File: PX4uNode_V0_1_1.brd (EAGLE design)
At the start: 45.4 x 34 mm, 134 parts, among them M3_MOUNT1101 MOUNT-HOLE3.1MM, M3_MOUNT1102 MOUNT-HOLE3.1MM, M3_MOUNT1103 MOUNT-HOLE3.1MM, M3_MOUNT1104 MOUNT-HOLE3.1MM, U101 STM32F4X7VX, U401 MAX3051, U402 MAX3051, X101 3.2x2.5 mm / 24 MHz / 15 ppm

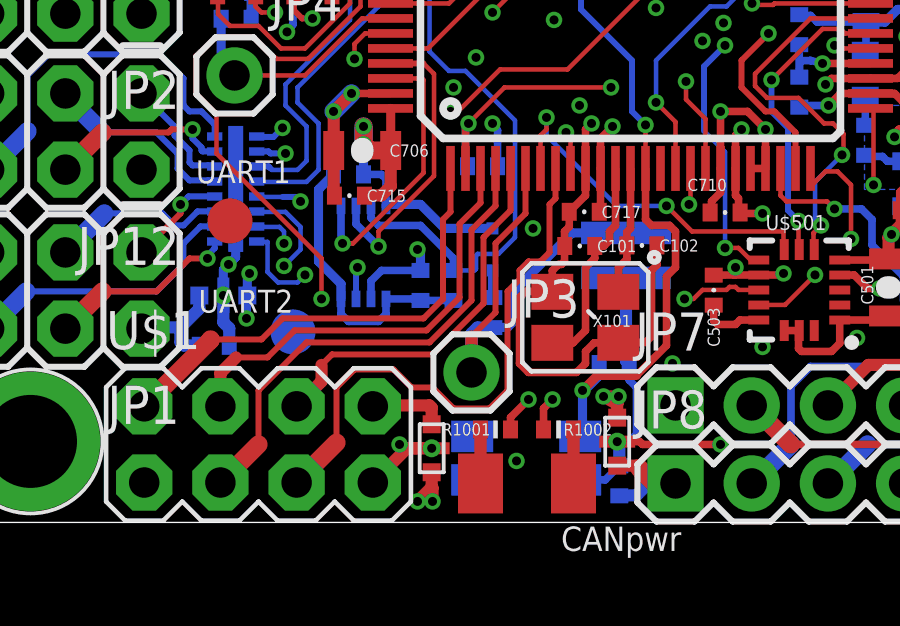
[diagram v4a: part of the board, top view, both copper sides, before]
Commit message: Removed extra Vbat hole
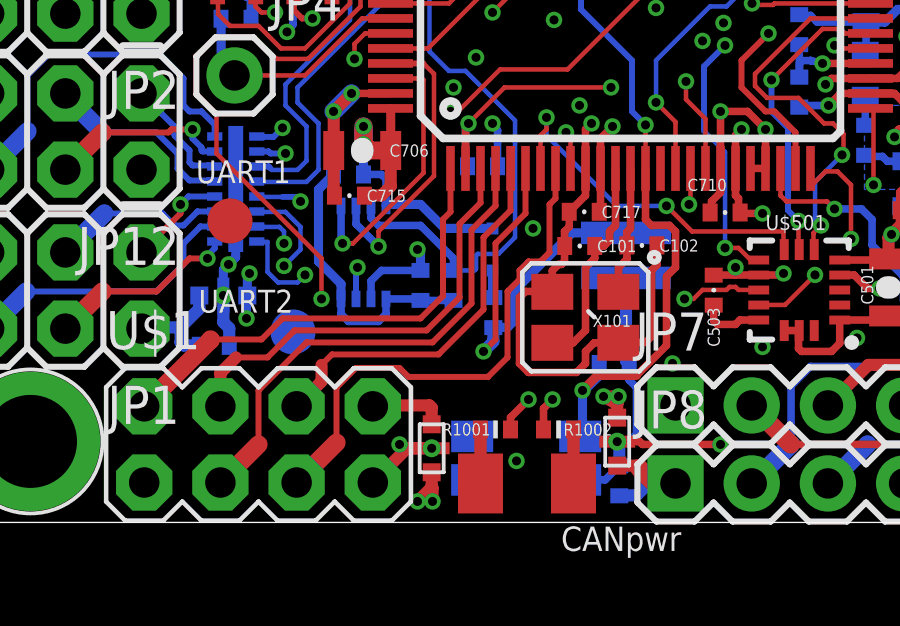
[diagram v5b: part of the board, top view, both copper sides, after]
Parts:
- removed JP3: M01PTH, SparkFun-Connectors:1X01
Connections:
- net VBAT: no longer JP3.1
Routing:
- net VBAT: track 16.0 -> 13.9 mm, vias 0 -> 1
- net GPIO_EXT_1: track 18.8 -> 17.3 mm
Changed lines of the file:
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@@
 <layer number="1" name="Top" color="4" fill="1" visible="yes" active="yes"/>
 <layer number="2" name="Ground" color="2" fill="10" visible="no" active="yes"/>
-<layer number="3" name="Horizontal" color="13" fill="15" visible="no" active="yes"/>
+<layer number="3" name="Horizontal" color="13" fill="15" visible="yes" active="yes"/>
 <layer number="4" name="Route4" color="1" fill="4" visible="no" active="no"/>
 <layer number="5" name="Route5" color="4" fill="4" visible="no" active="no"/>
@@
 <layer number="12" name="Route12" color="1" fill="5" visible="no" active="no"/>
 <layer number="13" name="Route13" color="4" fill="5" visible="no" active="no"/>
-<layer number="14" name="Vertical" color="14" fill="15" visible="no" active="yes"/>
+<layer number="14" name="Vertical" color="14" fill="15" visible="yes" active="yes"/>
 <layer number="15" name="Power" color="11" fill="15" visible="no" active="yes"/>
 <layer number="16" name="Bottom" color="1" fill="1" visible="yes" active="yes"/>
@@
 <attribute name="PARTNO" value="RC0402FR-0710KL" x="45.4" y="28.5" size="1.778" layer="27" rot="R180" display="off"/>
 </element>
-<element name="JP3" library="SparkFun-Connectors" package="1X01" value="M01PTH" x="30.2" y="9.2"/>
 <element name="JP4" library="SparkFun-Connectors" package="1X01" value="M01PTH" x="22.3" y="19.1"/>
 <element name="U$2" library="PX4lite" package="VSSOP8" value="74LVC2G240" x="26.6" y="13.2" rot="MR0"/>
@@
 <contactref element="U101" pad="4"/>
 <contactref element="U$1" pad="3"/>
-<wire x1="30.2" y1="11.6" x2="28.8" y2="10.2" width="0.2" layer="1"/>
-<wire x1="28.8" y1="10.2" x2="24.7" y2="10.2" width="0.2" layer="1"/>
+<wire x1="30.2" y1="11.5" x2="28.9" y2="10.2" width="0.2" layer="1"/>
+<wire x1="28.9" y1="10.2" x2="24.7" y2="10.2" width="0.2" layer="1"/>
 <wire x1="24.7" y1="10.2" x2="23.1" y2="8.6" width="0.2" layer="1"/>
 <wire x1="23.1" y1="8.6" x2="23.1" y2="6.8" width="0.2" layer="1"/>
-<wire x1="30.2" y1="11.6" x2="30.2" y2="13.95" width="0.2" layer="1"/>
+<wire x1="30.2" y1="11.5" x2="30.2" y2="13.95" width="0.2" layer="1"/>
 <wire x1="30.2" y1="13.95" x2="31" y2="14.75" width="0.2" layer="1"/>
 <wire x1="31" y1="14.75" x2="31" y2="16" width="0.2" layer="1"/>
@@
 <contactref element="U101" pad="5"/>
 <contactref element="U$1" pad="6"/>
-<wire x1="25.55" y1="9.8" x2="28.9" y2="9.8" width="0.2" layer="1"/>
-<wire x1="28.9" y1="9.8" x2="30.6" y2="11.5" width="0.2" layer="1"/>
-<wire x1="30.6" y1="11.5" x2="30.6" y2="13.7" width="0.2" layer="1"/>
+<wire x1="25.55" y1="9.8" x2="29.1" y2="9.8" width="0.2" layer="1"/>
+<wire x1="29.1" y1="9.8" x2="30.6" y2="11.3" width="0.2" layer="1"/>
+<wire x1="30.6" y1="11.3" x2="30.6" y2="13.7" width="0.2" layer="1"/>
 <wire x1="30.6" y1="13.7" x2="31.5" y2="14.6" width="0.2" layer="1"/>
 <wire x1="31.5" y1="14.6" x2="31.5" y2="16" width="0.2" layer="1"/>
@@
 <wire x1="29.5" y1="16" x2="29.5" y2="14.55" width="0.2" layer="1"/>
 <wire x1="29.5" y1="14.55" x2="29.25" y2="14.3" width="0.2" layer="1"/>
-<wire x1="29.25" y1="14.3" x2="29.25" y2="11.65" width="0.2" layer="1"/>
-<wire x1="29.25" y1="11.65" x2="28.6" y2="11" width="0.2" layer="1"/>
-<wire x1="28.6" y1="11" x2="23.9" y2="11" width="0.2" layer="1"/>
+<wire x1="29.25" y1="14.3" x2="29.25" y2="11.75" width="0.2" layer="1"/>
+<wire x1="29.25" y1="11.75" x2="28.5" y2="11" width="0.2" layer="1"/>
+<wire x1="28.5" y1="11" x2="23.9" y2="11" width="0.2" layer="1"/>
 <wire x1="19.29" y1="8.07" x2="21.5" y2="10.28" width="0.6096" layer="1"/>
 <wire x1="21.5" y1="10.28" x2="21.5" y2="10.3" width="0.6096" layer="1"/>
@@
 <contactref element="U101" pad="6"/>
 <contactref element="R706" pad="P$1"/>
-<contactref element="JP3" pad="1"/>
 <wire x1="31" y1="13.5" x2="32" y2="14.5" width="0.2" layer="1"/>
 <wire x1="32" y1="14.5" x2="32" y2="16" width="0.2" layer="1"/>
-<wire x1="31" y1="13.5" x2="31" y2="11.2" width="0.2" layer="1"/>
-<wire x1="31" y1="11.2" x2="30.2" y2="10.4" width="0.2" layer="1"/>
-<wire x1="30.2" y1="10.4" x2="30.2" y2="9.2" width="0.4064" layer="1"/>
-<wire x1="30.9288" y1="10.6944" x2="30.3944" y2="10.6944" width="0.4064" layer="16"/>
-<wire x1="30.3944" y1="10.6944" x2="30.2" y2="10.5" width="0.4064" layer="16"/>
-<wire x1="30.2" y1="10.5" x2="30.2" y2="9.2" width="0.4064" layer="16"/>
+<wire x1="31" y1="13.5" x2="31" y2="10.3" width="0.2" layer="1"/>
+<wire x1="31" y1="10.3" x2="30.6" y2="9.9" width="0.2" layer="1"/>
 <contactref element="U$4" pad="1"/>
 <wire x1="35.35" y1="13.85" x2="33.55" y2="13.85" width="0.3048" layer="16"/>
@@
 <wire x1="31.4" y1="10.7" x2="30.9344" y2="10.7" width="0.3048" layer="16"/>
 <wire x1="30.9344" y1="10.7" x2="30.9288" y2="10.6944" width="0.3048" layer="16"/>
+<via x="30.6" y="9.9" extent="1-16" drill="0.3"/>
+<wire x1="30.9288" y1="10.6944" x2="30.9288" y2="10.2288" width="0.4064" layer="16"/>
+<wire x1="30.9288" y1="10.2288" x2="30.6" y2="9.9" width="0.4064" layer="16"/>
 </signal>
 <signal name="N$11">
@@
 <wire x1="31.8" y1="12.3" x2="31.4" y2="11.9" width="0.2" layer="1"/>
 <wire x1="25.7" y1="6.86" x2="25.7" y2="8.7" width="0.2" layer="1"/>
-<wire x1="25.7" y1="8.7" x2="26.3" y2="9.3" width="0.2" layer="1"/>
-<wire x1="26.3" y1="9.3" x2="27.6" y2="9.3" width="0.2" layer="1"/>
-<wire x1="27.6" y1="9.3" x2="28.2" y2="8.7" width="0.2" layer="1"/>
-<wire x1="28.2" y1="8.7" x2="28.9" y2="8.7" width="0.2" layer="1"/>
-<wire x1="28.9" y1="8.7" x2="29.6" y2="8" width="0.2" layer="1"/>
-<wire x1="29.6" y1="8" x2="30.8" y2="8" width="0.2" layer="1"/>
-<wire x1="30.8" y1="8" x2="31.4" y2="8.6" width="0.2" layer="1"/>
-<wire x1="31.4" y1="8.6" x2="31.4" y2="11.9" width="0.2" layer="1"/>
+<wire x1="25.7" y1="8.7" x2="26.35" y2="9.35" width="0.2" layer="1"/>
+<wire x1="26.35" y1="9.35" x2="27.8" y2="9.35" width="0.2" layer="1"/>
+<wire x1="27.8" y1="9.35" x2="28.1" y2="9.05" width="0.2" layer="1"/>
+<wire x1="28.1" y1="9.05" x2="30.75" y2="9.05" width="0.2" layer="1"/>
+<wire x1="30.75" y1="9.05" x2="31.4" y2="9.7" width="0.2" layer="1"/>
+<wire x1="31.4" y1="9.7" x2="31.4" y2="11.9" width="0.2" layer="1"/>
 <wire x1="24.37" y1="5.53" x2="25.7" y2="6.86" width="0.6096" layer="1"/>
 </signal>

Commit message: Tweaks
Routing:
- net FMU-I2C1_SCL: track 15.8 -> 16.4 mm
- net GND: track 236.3 -> 236.4 mm, vias 31 -> 32
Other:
- board text added: "CAN5V"
- board text removed: "CANpwr"
